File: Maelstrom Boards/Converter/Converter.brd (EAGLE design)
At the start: 101.6 x 101.6 mm, 37 parts, among them Q1 BSS295, Q2 BSS295, Q3 BSS295

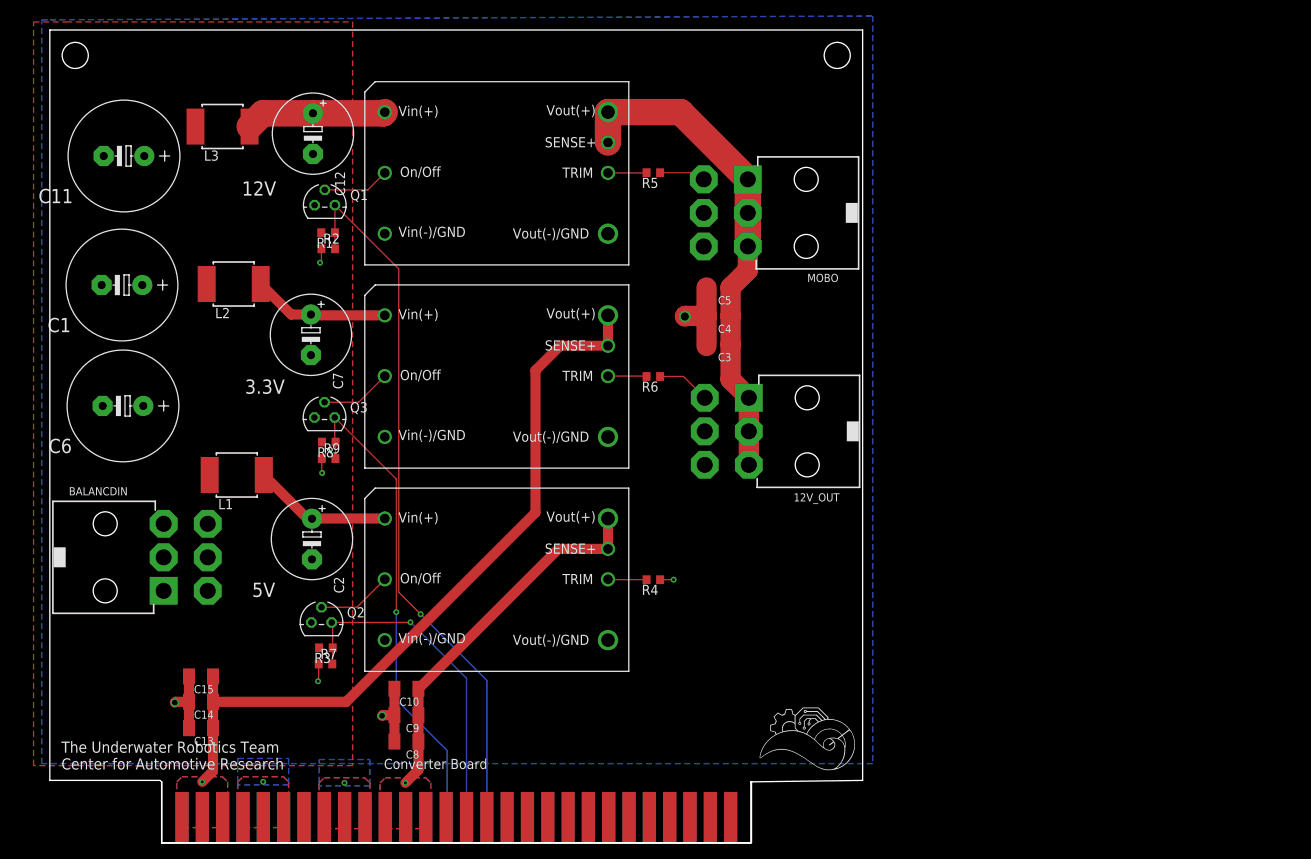
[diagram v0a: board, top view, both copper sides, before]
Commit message: Began routing on converter board
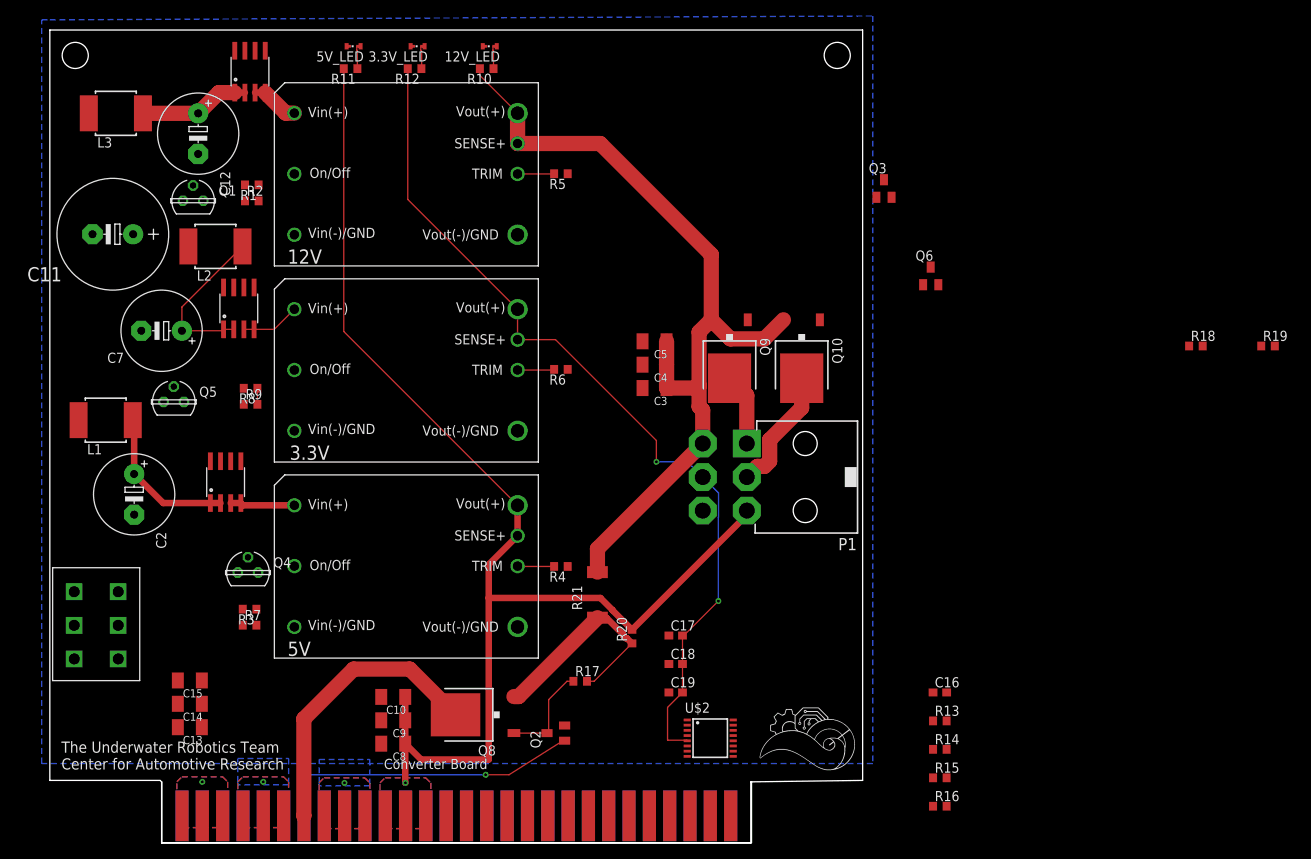
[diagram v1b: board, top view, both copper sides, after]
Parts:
- removed 12V_OUT, BALANCDIN, MOBO: (no value), con-molex-mini-fit:39-30-?06?
- removed C1, C6: 1000 uF, rcl:E5-13
- added 12V_LED, 3.3V_LED, 5V_LED: (no value), led:CHIPLED-0603-TTW
- added 1C, 1C1, 1C2: ACS722, ACS722:SOIC-8
- added C16, C17, C18, C19: (no value), rcl:C0603
- added P1: 39-30-06?, con-molex-mini-fit:39-30-?06?
- added Q10, Q8, Q9: FDD4141TO252, transistor-fet:TO252
- added Q4, Q5: VN10KM, transistor-fet:TO237
- added Q6: BSS123, transistor-small-signal:SOT23
- added R10, R11, R12: (no value), rcl:R0603
- added R13, R14, R15, R16, R17, R18, R19, R20: (no value), resistor:R0603
- added R21: (no value), resistor:M2309
- added U$2: ADC128D818, ADC128D818:TSSOP-16
- added U$3: 6PIN-VERT, Vertical_Connectors:6PIN_VERT
- Q1: value BSS295 -> VN10KM; device transistor-fet:TO92 -> transistor-fet:TO237
- Q2, Q3: value BSS295 -> BSS123; device transistor-fet:TO92 -> transistor-small-signal:SOT23
- R4: value 4.47 K -> 4.95 K
- moved Q3 75.6 mm to (104.3, 81.8)
- moved Q2 32.4 mm to (63.2, 13.7), turned to 90 degrees
- moved C2 22.9 mm to (10.5, 43.6)
- moved C7 18.7 mm to (14.0, 64.0), turned to 180 degrees
- moved L1 17.8 mm to (6.99, 52.8)
- moved Q1 16.5 mm to (17.9, 80.3)
- moved C12 14.4 mm to (18.5, 88.6)
- moved L3 13.4 mm to (8.26, 91.2)
- moved R9 11.9 mm to (25.1, 54.8)
- moved R8 11.9 mm to (25.1, 56.8)
- moved R4 11.7 mm to (63.9, 34.5)
- moved R6 11.6 mm to (63.9, 59.2)
- moved R5 11.6 mm to (63.9, 83.6)
- moved 5VCONVERTER 11.4 mm to (28.1, 23.1)
- moved 3.3VCONVERTER 11.3 mm to (28.1, 47.6)
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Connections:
- removed net 3.3VFILTERED: 3.3VCONVERTER.1,VIN(+), C7.+, L2.2
- new net 12VMONITORED: 12VCONVERTER.1,VIN(+), 1C1.IP-1, 1C1.IP-2
- new net 3V3FILTERED: 1C2.IP+1, 1C2.IP+2, C7.+, L2.2
- new net 3V3MONITORED: 1C2.IP-1, 1C2.IP-2, 3.3VCONVERTER.1,VIN(+)
- new net 5VMONITORED: 1C.IP-1, 1C.IP-2, 5VCONVERTER.1,VIN(+)
- new net JETSON_ON/OFF: Q6.1, U$1.18
- new net JETSON_SWITCHED: P1.2, Q10.3
- new net MOBO_ON/OFF: Q3.1, U$1.19
- new net MOBO_SWITCHED: P1.1, Q9.3
- new net N$10: Q8.2, R17.2, R20.1, R21.1
- new net N$11: 1C.VIOUT, U$2.IN2
- new net N$12: 1C1.VIOUT, U$2.IN1
- new net N$13: 1C2.VIOUT, U$2.IN0
- new net N$14: Q10.1, Q6.3, R19.1
- new net N$44: R13.2, R14.1, U$2.A0
- new net N$46: R15.1, R16.2, U$2.A1
- new net N$5: 12V_LED.A@1, R10.1
- new net N$6: 5V_LED.A@1, R11.1
- new net N$7: 3.3V_LED.A@1, R12.1
- new net N$8: Q2.3, Q8.1, R17.1
- new net N$9: Q3.3, Q9.1, R18.1
- new net PLTA_ON/OFF: Q2.1, U$1.7
- new net PLTA_SWITCHED: Q8.3, U$1.50
- new net SCL: U$1.31, U$2.SCL
- new net SDA: U$1.32, U$2.SDA
- net +12V: now also P1.4, Q10.2, Q9.2, R10.2, R18.2, R19.2, R21.2; no longer 12V_OUT.1, 12V_OUT.2, 12V_OUT.3, MOBO.1, MOBO.2, MOBO.3
- net +3V3: now also 1C.VCC, 1C1.VCC, 1C2.VCC, C16.1, C17.2, C18.2, C19.2, P1.5, R12.2, R13.1, R16.1, U$2.V+
- net +5V: now also P1.3, R11.2, R20.2
- net 12VFILTERED: now also 1C1.IP+1, 1C1.IP+2; no longer 12VCONVERTER.1,VIN(+)
- net 12VON: now also Q1.2; no longer Q1.1
- net 12VON-CON: now also Q1.1; no longer Q1.2
- net 3.3VON: now also Q5.2; no longer Q3.1
- net 3.3VON-CON: now also Q5.1; no longer Q3.2
- net 5VFILTERED: now also 1C.IP+1, 1C.IP+2; no longer 5VCONVERTER.1,VIN(+)
- net 5VON: now also Q4.2; no longer Q2.1
- net 5VON-CON: now also Q4.1; no longer Q2.2
- net AGND: now also 12V_LED.C@1, 1C.BW_SEL, 1C.GND, 1C1.BW_SEL, 1C1.GND, 1C2.BW_SEL, 1C2.GND, 3.3V_LED.C@1, 5V_LED.C@1, C16.2, C17.1, C18.1, C19.1, P1.6, Q2.2, Q3.2, Q4.3, Q5.3, Q6.2, R14.2, R15.2, U$2.GND, U$3.1+, U$3.1-, U$3.2-; no longer 12V_OUT.4, 12V_OUT.5, 12V_OUT.6, BALANCDIN.4, BALANCDIN.5, BALANCDIN.6, C1.-, C6.-, MOBO.4, MOBO.5, MOBO.6, Q2.3, Q3.3
- net V+: now also U$3.2+, U$3.3+, U$3.3-; no longer BALANCDIN.1, BALANCDIN.2, BALANCDIN.3, C1.+, C6.+
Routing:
- net +5V: track 47.2 -> 159.3 mm
- net 12VON: track 89.9 -> 0.03 mm, vias 1 -> 0
- net 3.3VON: track 61.0 -> 2.17 mm, vias 1 -> 0
- net AGND: track 46.7 -> 0.00 mm, vias 9 -> 2
- net +12V: track 62.5 -> 108.3 mm
- net 5VON: track 42.4 -> 0.03 mm, vias 1 -> 0
- net PLTA_ON/OFF: track 0.00 -> 39.0 mm, vias 0 -> 1
- net PLTA_SWITCHED: track 0.00 -> 36.0 mm
- net N$10: track 0.00 -> 27.8 mm
- net 3V3FILTERED: track 0.00 -> 20.2 mm
- net 3.3VFILTERED: track 17.1 -> 0.00 mm
- net JETSON_SWITCHED: track 0.00 -> 15.7 mm
- net +3V3: track 95.8 -> 110.3 mm, vias 1 -> 3
- net N$8: track 0.00 -> 12.4 mm
- net 5VON-CON: track 9.36 -> 0.00 mm
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- removed copper zone on layer 1, net V+
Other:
- outline, holes or cut-outs redrawn

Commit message: Converter board completed
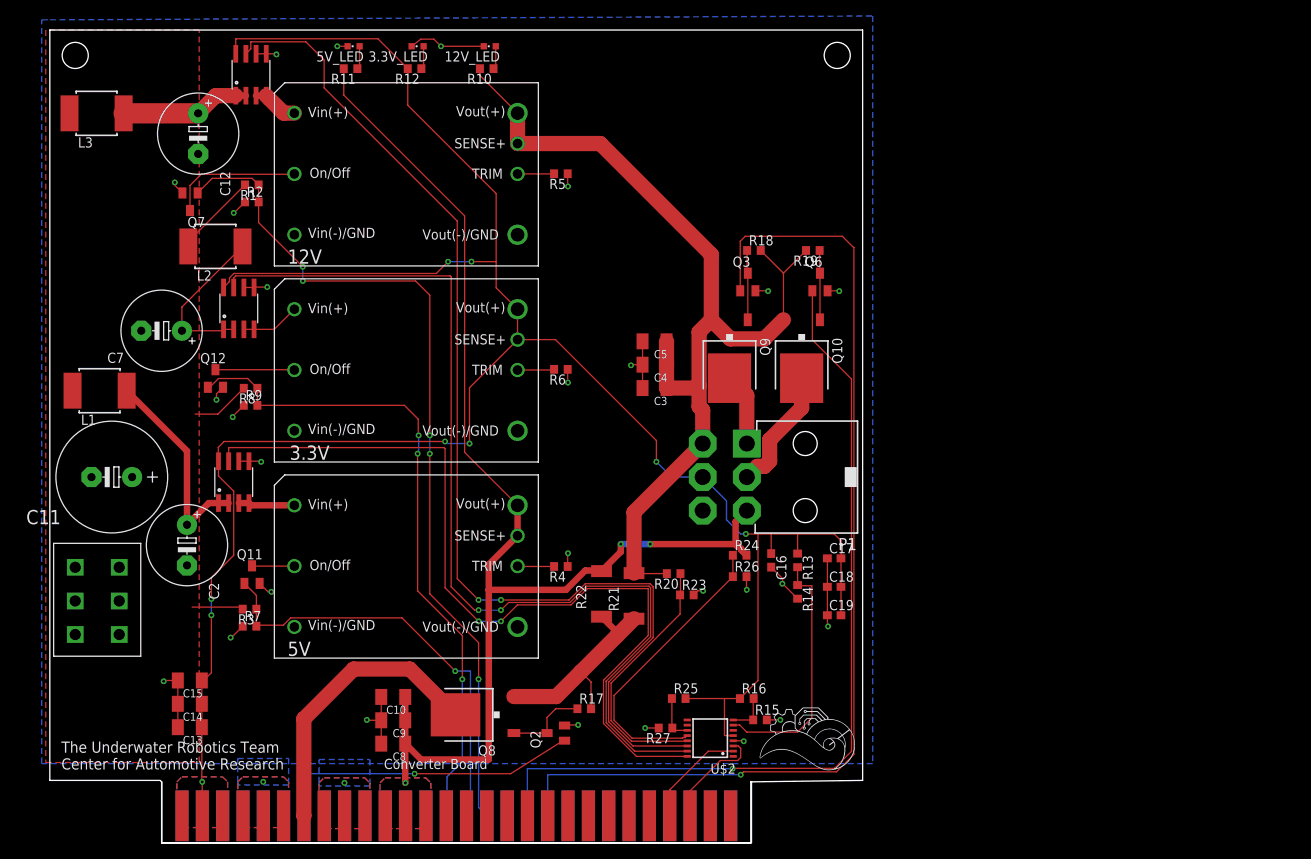
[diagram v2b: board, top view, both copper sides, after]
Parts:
- removed Q1, Q4, Q5: VN10KM, transistor-fet:TO237
- added Q11, Q12, Q7: BSS123, transistor-small-signal:SOT23
- added R22: (no value), resistor:M2309
- added R23, R24, R25, R26, R27: (no value), resistor:R0603
- 12V_LED, 3.3V_LED, 5V_LED: device led:CHIPLED-0603-TTW -> led:CHIPLED_0603
- moved R19 58.1 mm to (95.4, 74.0), turned to 180 degrees
- moved R18 56.5 mm to (88.0, 74.0)
- moved C11 30.4 mm to (7.75, 45.7)
- moved R16 27.6 mm to (87.1, 18.0)
- moved R13 26.8 mm to (93.5, 35.3), turned to 270 degrees
- moved C16 26.8 mm to (90.2, 35.3), turned to 270 degrees
- moved R14 26.5 mm to (93.5, 31.4), turned to 270 degrees
- moved R15 23.6 mm to (88.8, 15.4)
- moved C17 22.0 mm to (98.0, 35.6)
- moved C18 22.0 mm to (98.0, 32.0)
- moved C19 22.0 mm to (98.0, 28.4)
- moved Q3 20.6 mm to (87.2, 70.1)
- moved Q6 13.9 mm to (96.3, 70.1)
- moved R20 9.44 mm to (78.0, 33.7), turned to 180 degrees
- moved C2 9.16 mm to (17.1, 37.2)
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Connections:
- removed net 12VON-CON: 12VCONVERTER.2,ON/OFF, Q1.1
- removed net 3.3VON-CON: 3.3VCONVERTER.2,ON/OFF, Q5.1
- removed net 5VON-CON: 5VCONVERTER.2,ON/OFF, Q4.1
- new net N$15: R20.1, R23.1, U$2.IN3
- new net N$16: R24.1, R26.1, U$2.IN4
- new net N$17: R25.1, R27.1, U$2.IN5
- new net N$18: 12VCONVERTER.2,ON/OFF, Q7.3
- new net N$19: 5VCONVERTER.2,ON/OFF, Q11.3
- new net N$4: 3.3VCONVERTER.2,ON/OFF, Q12.3
- net +12V: now also R20.2
- net +3V3: now also R25.2
- net +5V: now also R22.2, R24.2; no longer R20.2
- net 12VON: now also Q7.1; no longer Q1.2
- net 3.3VON: now also Q12.1; no longer Q5.2
- net 5VON: now also Q11.1; no longer Q4.2
- net AGND: now also 12V_LED.C, 3.3V_LED.C, 5V_LED.C, Q11.2, Q12.2, Q7.2, R23.2, R26.2, R27.2; no longer 12V_LED.C@1, 3.3V_LED.C@1, 5V_LED.C@1, Q1.3, Q4.3, Q5.3
- net N$10: now also R22.1; no longer R20.1
- net N$11: now also U$2.IN0; no longer U$2.IN2
- net N$12: now also U$2.IN2; no longer U$2.IN1
- net N$13: now also U$2.IN1; no longer U$2.IN0
- net N$5: now also 12V_LED.A; no longer 12V_LED.A@1
- net N$6: now also 5V_LED.A; no longer 5V_LED.A@1
- net N$7: now also 3.3V_LED.A; no longer 3.3V_LED.A@1
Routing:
- net +3V3: track 110.3 -> 298.2 mm, vias 3 -> 9
- net N$12: track 0.00 -> 140.4 mm, vias 0 -> 2
- net MOBO_ON/OFF: track 0.00 -> 129.1 mm, vias 0 -> 1
- net N$13: track 0.00 -> 125.5 mm, vias 0 -> 2
- net 12VON: track 0.03 -> 107.7 mm, vias 0 -> 5
- net JETSON_ON/OFF: track 0.00 -> 106.9 mm, vias 0 -> 1
- net N$11: track 0.00 -> 106.4 mm, vias 0 -> 2
- net AGND: track 0.00 -> 85.0 mm, vias 2 -> 29
- net 3.3VON: track 2.17 -> 83.1 mm, vias 0 -> 3
- net 5VON: track 0.03 -> 54.2 mm, vias 0 -> 1
- net N$16: track 0.00 -> 37.0 mm
- net N$15: track 0.00 -> 32.6 mm
- net N$44: track 0.00 -> 31.5 mm
- net V+: track 0.00 -> 24.5 mm
- net N$18: track 0.00 -> 16.8 mm
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- added copper zone on layer 1, net V+
